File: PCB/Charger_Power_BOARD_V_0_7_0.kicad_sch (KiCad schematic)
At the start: 58 parts, among them J1 AMT0440005TH0000G, J10 AMT0440005TH0000G, J11 AMT0440005TH0000G, J12 AMT0440005TH0000G, J13 AMT0440005TH0000G, J14 AMT0440005TH0000G, J15 AMT0440005TH0000G, J18 Conn_01x03_Pin, J19 Screw_Terminal_01x02, J21 Screw_Terminal_01x02, J3 AMT0440005TH0000G, J4 Conn_01x04_Socket, J5 AMT0440005TH0000G, J6 B6B-XH-A_LF__SN_, J7 AMT0440005TH0000G, J8 Conn_01x02_Socket, J9 B6B-XH-A_LF__SN_, K5 Relay_IM_NE801A, K6 Relay_IM_NE801A, Q5 BSS316N H6327, Q6 BSS316N H6327, SW2 SW_SPST, U1 THVD1400DR, U11 DRV8220DRL, U8 RCD MD0630STA-P

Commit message: Implementação do novo circuito do Wleding detector; correcao dos campos dos componentes
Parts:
- removed J21: Screw_Terminal_01x02, TerminalBlock_Phoenix:TerminalBlock_Phoenix_MKDS-3-2-5.08_1x02_P5.08mm_Horizontal, symbol Connector:Screw_Terminal_01x02
- C1: Distribuidor Mouser -> (none); Link https://pt.mouser.com/ProductDetail/TAIYO-YUDEN/GMK316AB710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 -> (none); MPN (none) -> GMK316AB7106KL-TR; Ref GMK316AB7106KL-TR -> (none)
- C103, R141, R142: Distribuidor Mouser -> (none)
- C2, C84: Distribuidor Mouser -> (none); Link https://pt.mouser.com/ProductDetail/Samsung-Electro-Mechani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 -> (none); MPN (none) -> CL10B104MB8NNNC; Ref CL10B104MB8NNNC -> (none)
- D1: Distribuidor Mouser -> (none); Link https://pt.mouser.com/ProductDetail/Bourns/CDSOT23-SM712?qs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 -> (none); MPN (none) -> CDSOT23-SM712; Ref CDSOT23-SM712 -> (none)
- D18, D22: Distribuidor Mouser -> (none); Link https://pt.mouser.com/ProductDetail/Vishay-General-Semicond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 -> (none); MPN (none) -> SS12-E3/61T; Ref SS12-E3/61T -> (none)
- J1, J10, J11, J12, J13, J14, J15, J3, J5, J7: Height 7.4 -> (none); Manufacturer_Name Amphenol -> (none); Manufacturer_Part_Number AMT0440005TH0000G -> (none)
- J6, J9: Height 7 -> (none); Manufacturer_Name JST (JAPAN SOLDERLESS TERMINALS) -> (none); Manufacturer_Part_Number B6B-XH-A(LF)(SN) -> (none); Mouser Part Number 306-B6BXHALFSN -> (none); Mouser Price/Stock https://www.mouser.co.uk/ProductDetail/JST-Commercial/B6B-X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 -> (none)
- K5: footprint LIBRARY_KICAD:Relay_IM_NE801A -> FOOTPRINTS:Relay_IM_NE801A
- Q5, Q6: Distribuidor Mouser -> (none); Link https://pt.mouser.com/ProductDetail/Infineon-Technologies/B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 -> (none); MPN (none) -> BSS316N H6327; Ref BSS316N H6327 -> (none)
- R1, R105, R114, R27: Distribuidor Mouser -> (none); Link https://pt.mouser.com/ProductDetail/Vishay-Draloric/RCS0603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 -> (none); MPN (none) -> RCS060310K0FKEA; Ref RCS060310K0FKEA -> (none)
- R106: Distribuidor Mouser -> (none); Link https://pt.mouser.com/ProductDetail/Vishay/CRCW0603120RFKEA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 -> (none); MPN (none) -> CRCW0603120RFKEAC; Ref CRCW0603120RFKEAC -> (none)
- R110, R112: Distribuidor Mouser -> (none); Link https://pt.mouser.com/ProductDetail/Vishay/CRCW0603100RJNEA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 -> (none); MPN (none) -> CRCW0603100RJNEA; Ref CRCW0603100RJNEA -> (none)
- R2, R3: Distribuidor Mouser -> (none); Link https://pt.mouser.com/ProductDetail/Royalohm/0603WAF100JT1E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 -> (none); MPN (none) -> 0603WAF100JT1E; Ref 0603WAF100JT1E -> (none)
- SW2: Distribuidor Mouser -> (none); Link https://pt.mouser.com/ProductDetail/Omron-Electronics/B3U-1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 -> (none); MPN (none) -> B3U-1000PM; Ref B3U-1000PM -> (none)
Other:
- sheet MCU ports: added EN_WEL_DETEC; removed none
- sheet Welding_Contact_Detector ports: added ENABLE; removed none
- sheet Welding_Contact_Detector1 ports: added ENABLE; removed none
- sheet Welding_Contact_Detector2 ports: added ENABLE; removed none
- sheet Welding_Contact_Detector3 ports: added ENABLE; removed none
- moved on the sheet: C103, C84, H19, H5, H6, H7, H8, H9, J18, J19, R141, R142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

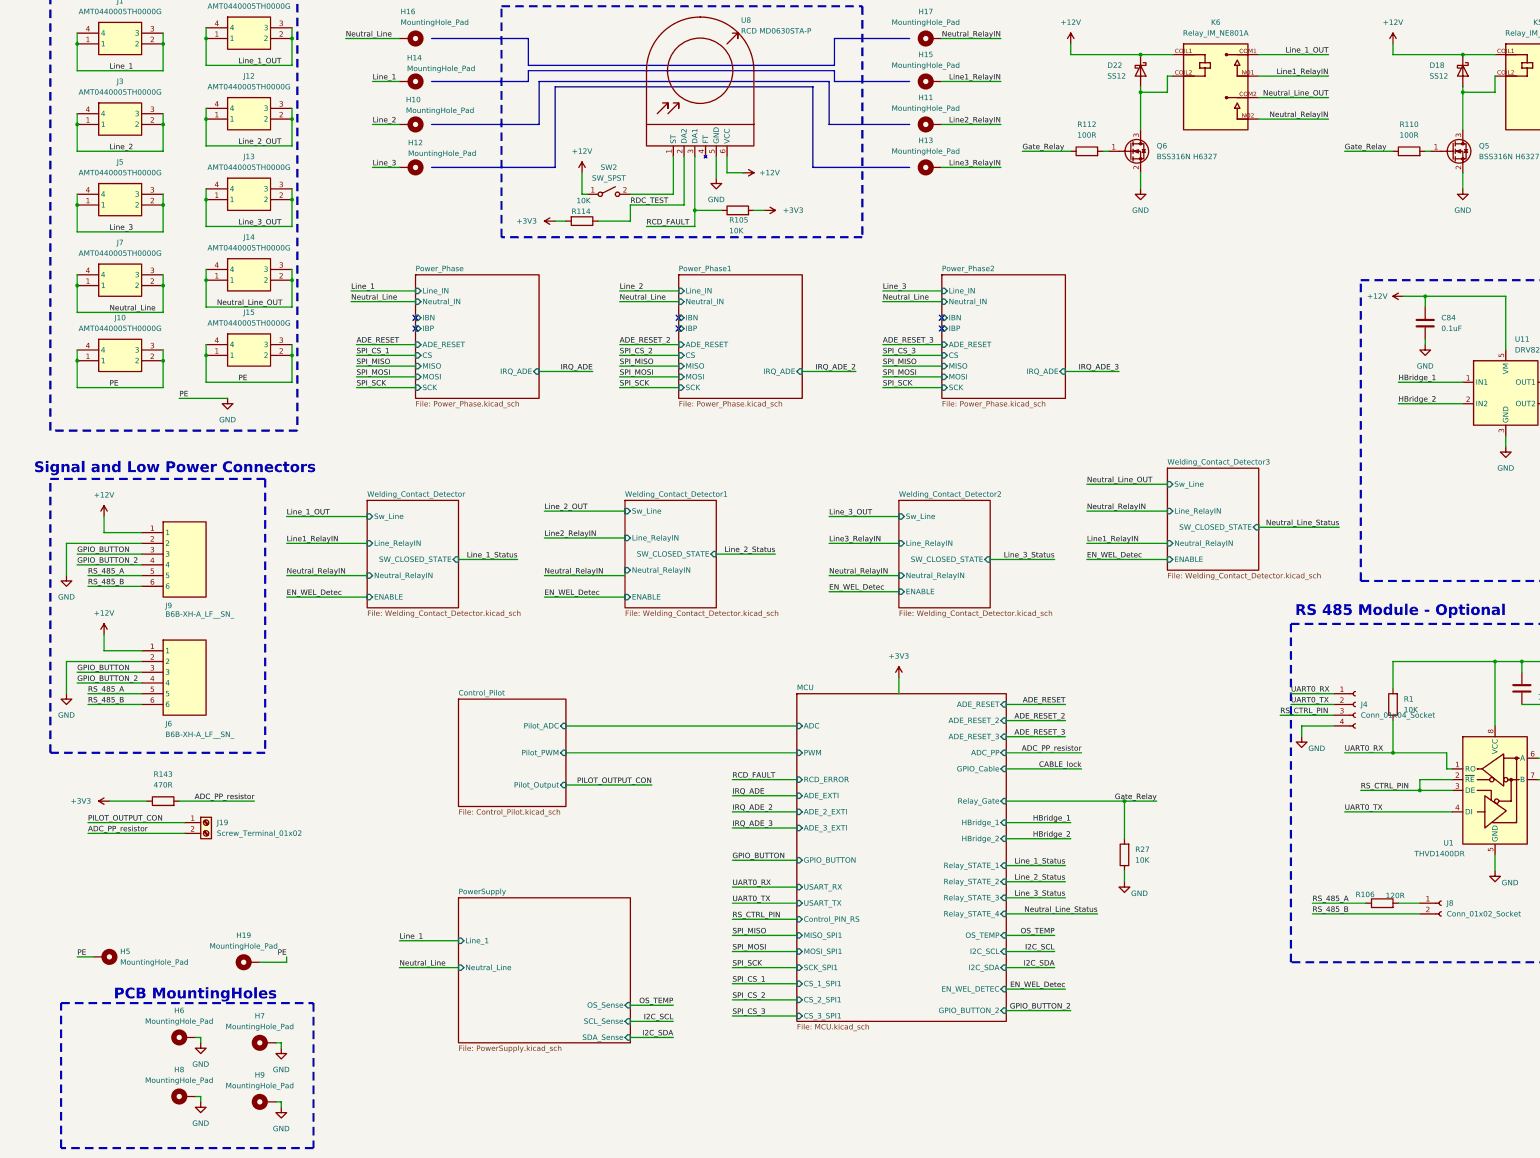
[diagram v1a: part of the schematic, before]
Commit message: Routing terminado; A corrigir violações; falta colocar as proteçãoes de inversão de polaridade; fusivél; TVS
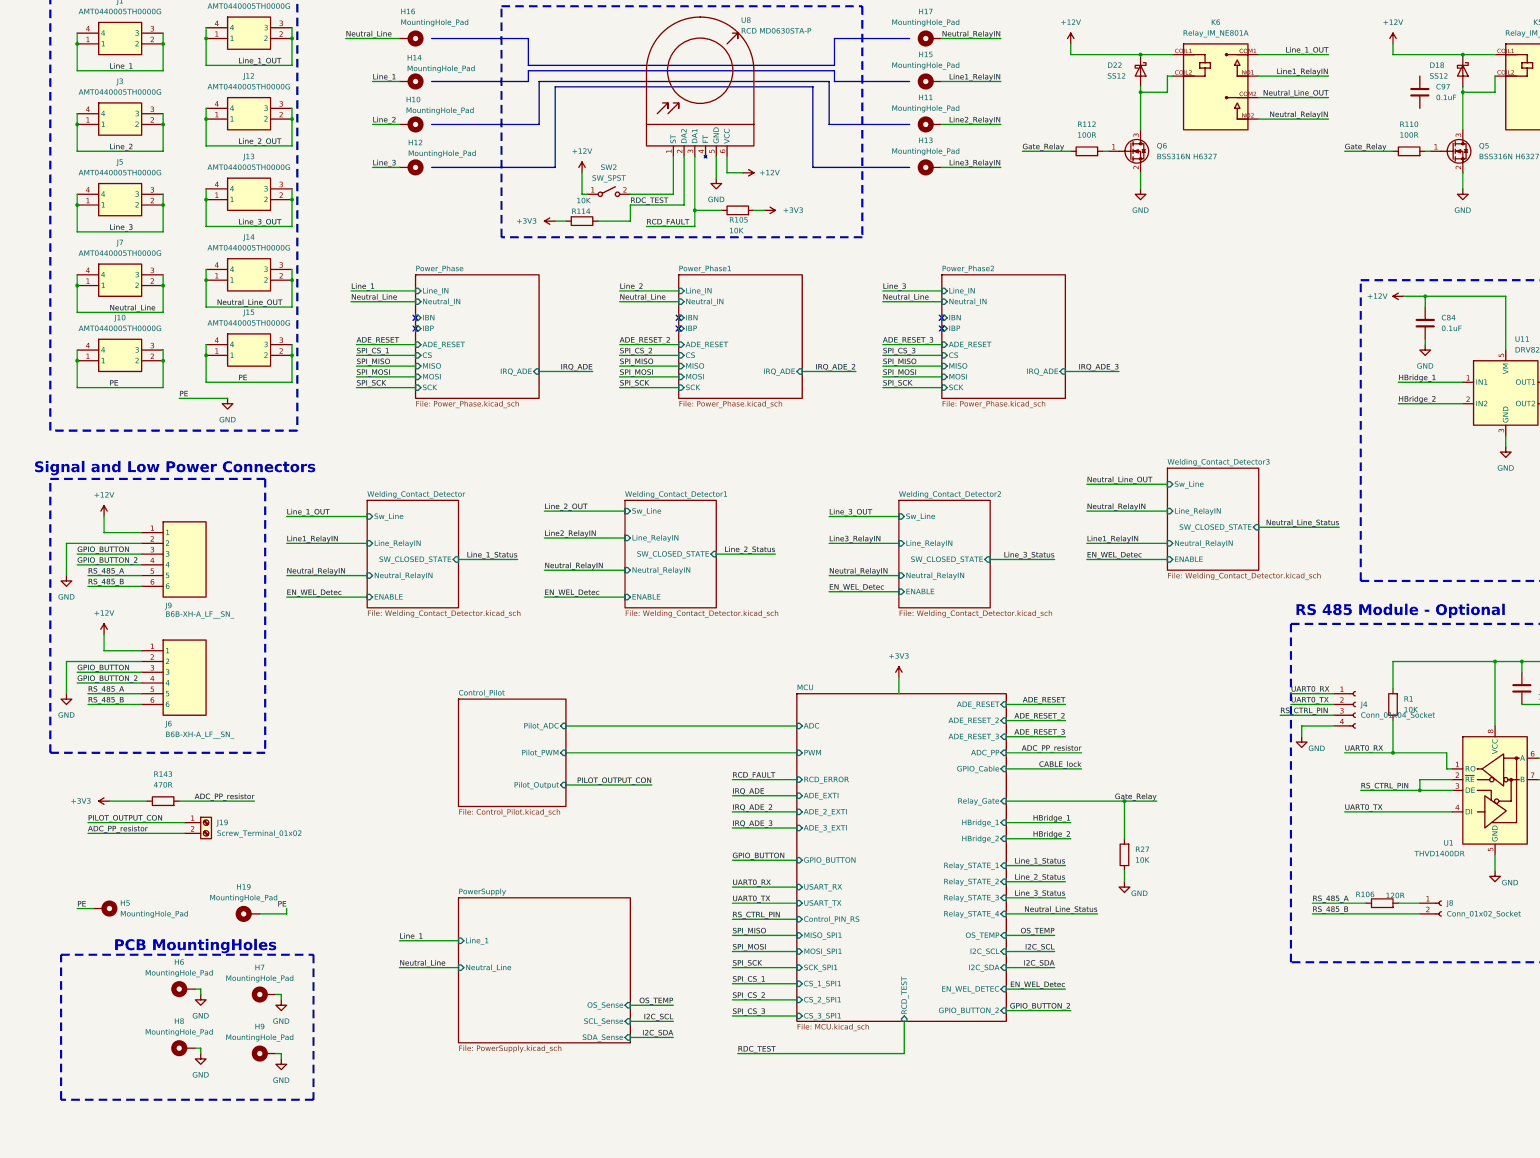
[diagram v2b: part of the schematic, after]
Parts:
- added C97: 0.1uF, Capacitor_SMD:C_0603_1608Metric, symbol Device:C
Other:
- sheet MCU ports: added RCD_TEST; removed none
- moved on the sheet: H19, H5, H6, H7, H8, H9

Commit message: pequena correção
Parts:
- added C100: 0.1uF, Capacitor_SMD:C_0603_1608Metric, symbol Device:C
- added C98, C99: 10uF, Capacitor_SMD:C_1206_3216Metric, symbol Device:C
- R110, R112: value 100R -> 470R; MPN CRCW0603100RJNEA -> (none)
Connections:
- net +12V: now also C97.1, C100.1, C98.1, C99.1
- net GND: now also C97.2, C100.2, C98.2, C99.2
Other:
- moved on the sheet: C97

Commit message: Layout finalizado
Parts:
- removed SW2: SW_SPST, Button_Switch_SMD:SW_SPST_B3U-1000P, symbol Switch:SW_SPST
- added Q1: BSS84, Package_TO_SOT_SMD:SOT-23, symbol Transistor_FET:BSS84
- added Q11: BSS316N H6327, Package_TO_SOT_SMD:SOT-23, symbol Transistor_FET:2N7002E
- added R120: 470R, Resistor_SMD:R_0603_1608Metric, symbol Device:R
- added R173: 120R, Resistor_SMD:R_0603_1608Metric, symbol Device:R
- added R28: 10K, Resistor_SMD:R_0603_1608Metric, symbol Device:R
- added R69, R84: 100K, Resistor_SMD:R_0603_1608Metric, symbol Device:R
- H9: footprint MountingHole:MountingHole_5.3mm_M5_DIN965_Pad_TopBottom -> MountingHole:MountingHole_5.3mm_M5
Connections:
- net +12V: now also Q1.2 (S), R69.1
- net GND: now also Q11.2 (S), R28.1; no longer H9.1
- net at U8.1 (ST): now also R173.2
- new net: Q11.1 (G), R120.2, R28.2
- new net: Q1.1 (G), R69.2, R84.1
- new net: Q11.3 (D), R84.2
- new net: Q1.3 (D), R173.1
- new net RCD_TEST_DRIVE: R120.1
- no-connect marks 6 -> 1
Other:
- sheet MCU ports: added RCD_TEST_DRIVE; removed none
- sheet PowerSupply ports: added none; removed Line_1, Neutral_Line
- moved on the sheet: R105, R114
